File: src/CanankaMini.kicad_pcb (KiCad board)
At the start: 2 copper layers, 44 x 16.5 mm, 21 parts, among them J1 48037-2200, J2 MC 1,5/4, Q1 Val**, Q2 Val**, U1 MCP2221, U2 PIC18F25K80, U3 MCP2561

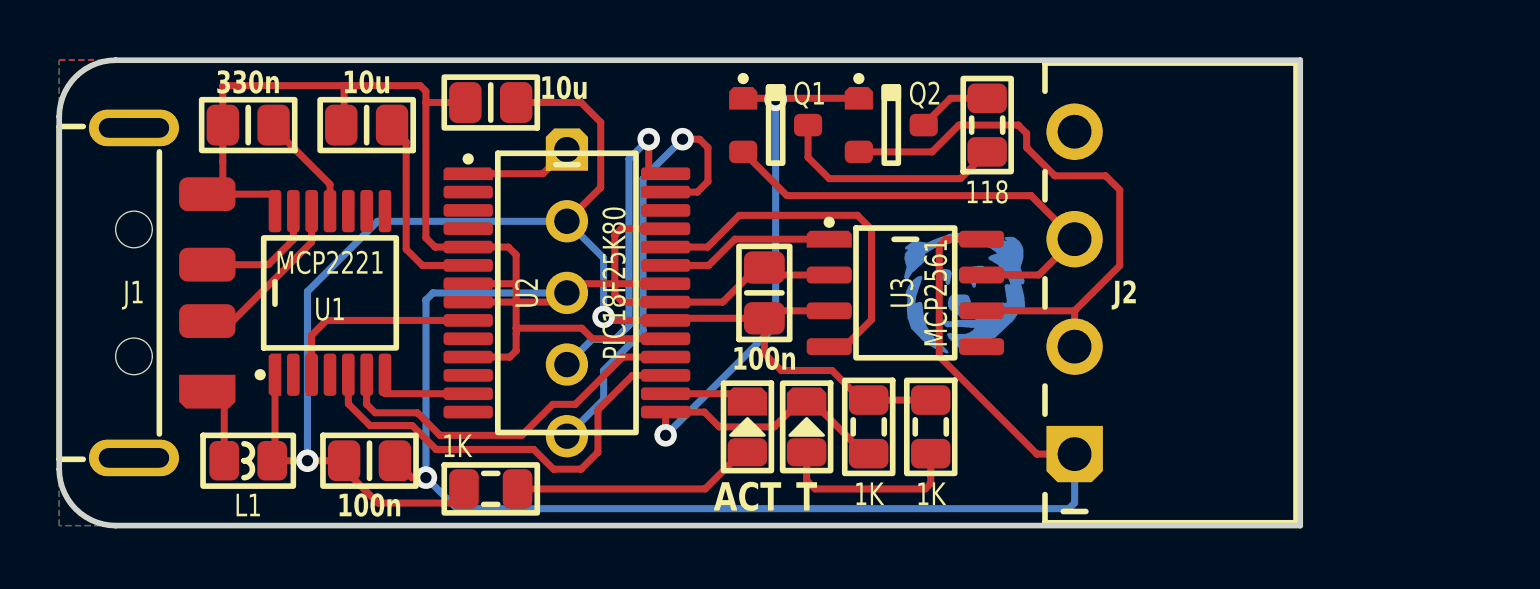
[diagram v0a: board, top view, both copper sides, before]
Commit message: Added current limiting
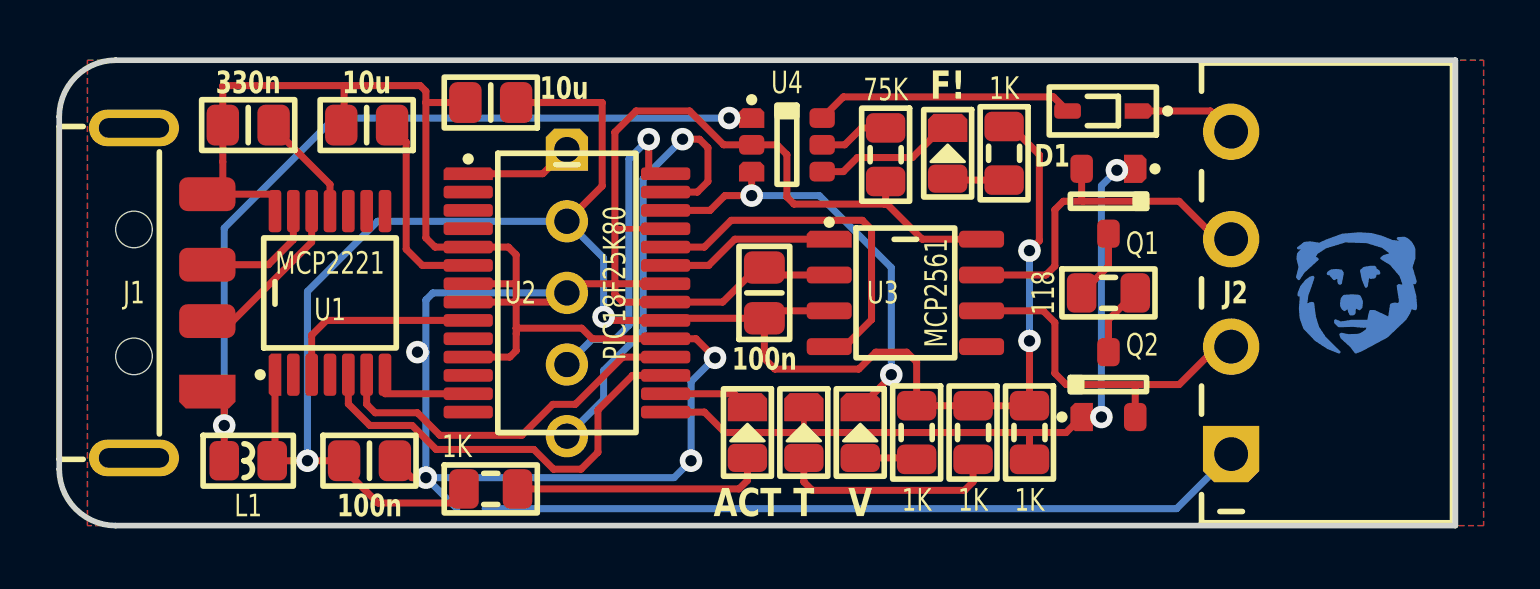
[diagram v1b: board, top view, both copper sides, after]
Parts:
- added D1: CUS08F30, Medo64:D (SOD323), F.Cu at (57.0, 21.8)
- added DS3: V, Medo64:DS (0805), F.Cu at (48.4, 33.2)
- added DS4: F!, Medo64:DS (0805), F.Cu at (51.5, 23.3)
- added R4: 1K, Medo64:R (0805), F.Cu at (52.4, 33.2)
- added R6: 1K, Medo64:R (0805), F.Cu at (53.5, 23.3)
- added R7: 75K, Medo64:R (0805), F.Cu at (49.3, 23.4)
- added U4: AP22652W6-7, Medo64:U LoadSwitch Adjustable [AP22653AW6-7] (SOT23-6), F.Cu at (45.8, 23.0)
- Q1, Q2: value Val** -> DMG2305UX-13
- moved ICON 13.9 mm to (66.0, 28.2)
- moved Q1 12.1 mm to (57.2, 25.0), turned to 180 degrees
- moved Q2 12.0 mm to (57.2, 31.5), turned to 0 degrees
- moved R1 7.34 mm to (57.2, 28.2), turned to 0 degrees
- moved R5 5.70 mm to (54.4, 33.2)
- moved J2 5.55 mm to (61.5, 28.2)
- moved R3 0.54 mm to (50.4, 33.2)
- moved DS2 0.22 mm to (46.4, 33.2)
- moved DS1 0.20 mm to (44.4, 33.2)
- renumbered R4 to R5
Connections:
- R3 pad 2: LED_CAN_TERMINATE -> LED_POWER
- U2 pad 26: (no net) -> POWER_ON#
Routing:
- net GND: track 105.2 -> 132.6 mm, vias 1 -> 4
- net USB_5V: track 2.66 -> 30.0 mm, vias 0 -> 2
- net 5V: track 53.1 -> 69.9 mm, vias 2 -> 4
- net POWER_ON#: track 0.00 -> 15.5 mm, vias 0 -> 2
- net OUT_5V: track 0.00 -> 9.22 mm
- net CAN_L: track 20.4 -> 12.2 mm
- net CAN_H_SPLIT: track 8.20 -> 2.49 mm
- net POWER_FAULT#: track 0.00 -> 4.89 mm
- net CAN_H: track 16.9 -> 12.3 mm
- net CAN_V+: track 0.00 -> 3.60 mm
- net ILIMIT: track 0.00 -> 2.50 mm
- net LED_POWER: track 0.00 -> 1.95 mm
- net LED_FAULT: track 0.00 -> 1.95 mm
- net LED_CAN_TERMINATE: track 6.66 -> 7.90 mm
- net IO_CONTROL_TERMINATE#: track 26.4 -> 27.4 mm
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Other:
- board size 44 x 16.5 mm -> 49.5 x 16.5 mm

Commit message: Adjusted current limiting
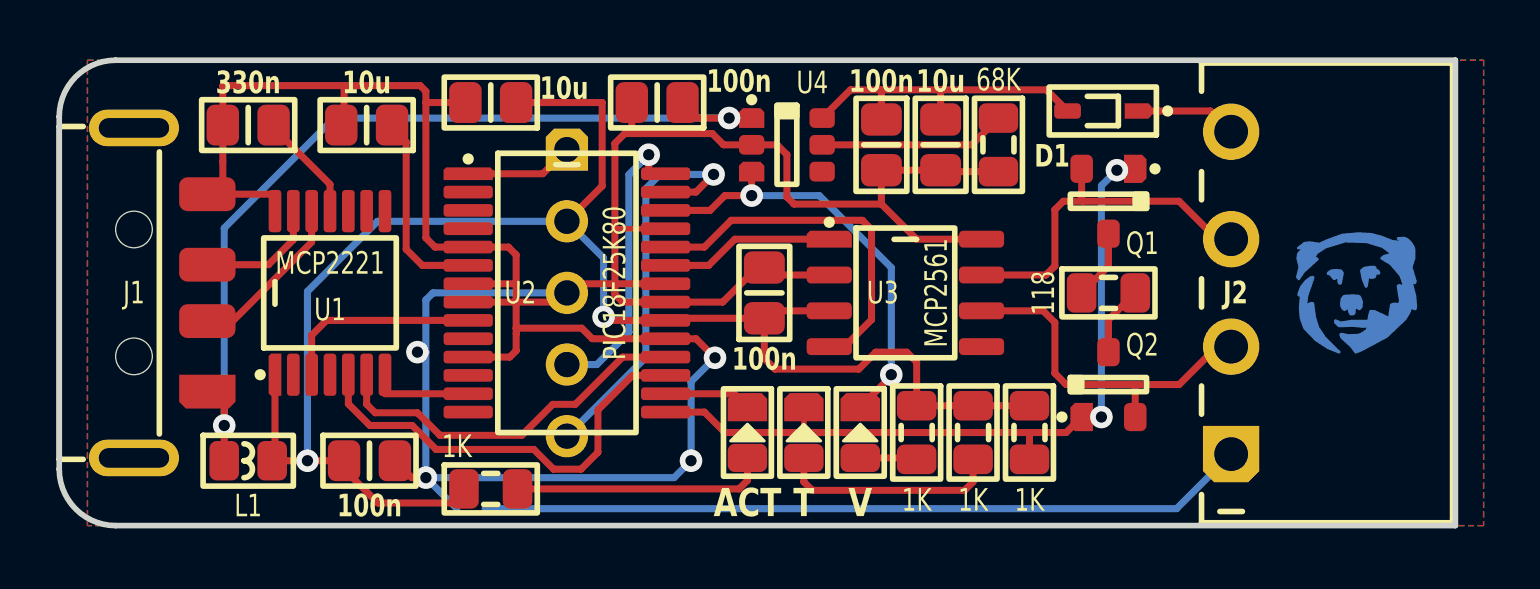
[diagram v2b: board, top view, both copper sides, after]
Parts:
- removed DS4: F!, Medo64:DS (0805)
- removed R6: 1K, Medo64:R (0805)
- added C3: 100n, Medo64:C (0805), F.Cu at (41.2, 21.5)
- added C4: 100n, Medo64:C (0805), F.Cu at (49.1, 23.0)
- added C8: 10u, Medo64:C (0805), F.Cu at (51.2, 23.0)
- R7: value 75K -> 68K
- U4: footprint Medo64:U LoadSwitch Adjustable [AP22653AW6-7] (SOT23-6) -> Medo64:U LoadSwitch Adjustable [AP22652W6-7] (SOT23-6)
- moved R7 4.02 mm to (53.3, 23.0)
- renumbered C3 to C5, C5 to C6, C4 to C7
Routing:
- net 5V: track 69.9 -> 58.7 mm, vias 4 -> 2
- net POWER_FAULT#: track 4.89 -> 0.00 mm
- net GND: track 132.6 -> 137.2 mm
- net ILIMIT: track 2.50 -> 6.64 mm
- net USB_5V: track 30.0 -> 32.7 mm
- net OUT_5V: track 9.22 -> 11.5 mm
- net LED_FAULT: track 1.95 -> 0.00 mm
- net ICSP_PGC: track 16.1 -> 14.5 mm
- net ICSP_PGD: track 10.9 -> 9.94 mm

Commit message: Fixing up component list
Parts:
- renumbered R7 to R6
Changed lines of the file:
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@@
 		(at 53.3 23 -90)
 		(tags "RESC2013X70N")
-		(property "Reference" "R7"
+		(property "Reference" "R6"
 			(at 0 -1.6 90)
 			(layer "F.SilkS")
